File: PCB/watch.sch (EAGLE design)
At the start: 5 parts

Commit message: base layout
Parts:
- removed U$2: 5-WAYSWITCH, 5-wayswitch:5-WAYSWITCH
- added C2: (no value), SparkFun:CAP0603
- added IC1: ISL1209, adafruit:ISL1209
- added Q1: IRFD9210, transistor-fet:IRFD9210
- added SP1: SPEAKER/PS12, adafruit:SPEAKER/PS12
- added U$3: 5-WAYSWITCH, 5-wayswitch:5-WAYSWITCH
- added U1: (no value), adafruit:GPS_FGPMMOPA6H
- added U2: MKL27Z256VLH4, Freescale:MKL27Z256VLH4
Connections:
- new net N$2: Q1.G, U2.PTC1/LLWU_P6/RTC_CLKIN
- new net N$4: U1.TX, U2.PTA19
- new net N$5: SP1.+, U2.PTE30
- new net N$6: Q1.D, U1.VCC
- new net PBT16: U1.3D-FIX
- new net PTB16: U2.PTB16
- net GND: now also C2.2, SP1.-, U$3.GND, U1.GND@1, U1.GND@2, U1.GND@3, U1.GND@4, U2.VSS, U2.VSS_3; no longer U$2.GND
- net V+: now also C2.1, Q1.S, U1.VBACKUP
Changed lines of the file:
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@@
 <layer number="54" name="bGND_GNDA" color="1" fill="9" visible="no" active="no"/>
 <layer number="56" name="wert" color="7" fill="1" visible="no" active="no"/>
+<layer number="57" name="tCAD" color="7" fill="1" visible="no" active="no"/>
 <layer number="90" name="Modules" color="5" fill="1" visible="yes" active="yes"/>
 <layer number="91" name="Nets" color="2" fill="1" visible="yes" active="yes"/>
@@
 <layer number="132" name="bAdjust" color="7" fill="1" visible="yes" active="yes"/>
 <layer number="144" name="Drill_legend" color="7" fill="1" visible="yes" active="yes"/>
+<layer number="150" name="Notes" color="7" fill="1" visible="no" active="yes"/>
 <layer number="151" name="HeatSink" color="7" fill="1" visible="yes" active="yes"/>
 <layer number="152" name="_bDocu" color="7" fill="1" visible="yes" active="yes"/>
+<layer number="153" name="FabDoc1" color="6" fill="1" visible="no" active="no"/>
+<layer number="154" name="FabDoc2" color="2" fill="1" visible="no" active="no"/>
+<layer number="155" name="FabDoc3" color="7" fill="15" visible="no" active="no"/>
 <layer number="199" name="Contour" color="7" fill="1" visible="yes" active="yes"/>
 <layer number="200" name="200bmp" color="1" fill="10" visible="yes" active="yes"/>
@@
 <part name="SUPPLY2" library="supply2" deviceset="GND" device=""/>
 <part name="SUPPLY3" library="supply2" deviceset="V+" device=""/>
-<part name="U$2" library="5-wayswitch" deviceset="5-WAYSWITCH" device=""/>
 <part name="SUPPLY4" library="supply2" deviceset="GND" device=""/>
+<part name="U1" library="adafruit" deviceset="GPS_FGPMMOPA6H" device=""/>
+<part name="SUPPLY5" library="supply2" deviceset="GND" device=""/>
+<part name="U2" library="Freescale" deviceset="MKL27Z256VLH4" device=""/>
+<part name="SUPPLY6" library="supply2" deviceset="GND" device=""/>
+<part name="SUPPLY7" library="supply2" deviceset="GND" device=""/>
+<part name="C2" library="SparkFun" deviceset="CAP" device="0603"/>
+<part name="SUPPLY8" library="supply2" deviceset="V+" device=""/>
+<part name="SUPPLY9" library="supply2" deviceset="GND" device=""/>
+<part name="SUPPLY10" library="supply2" deviceset="V+" device=""/>
+<part name="Q1" library="transistor-fet" deviceset="IRFD9210" device=""/>
+<part name="U$3" library="5-wayswitch" deviceset="5-WAYSWITCH" device=""/>
+<part name="SP1" library="adafruit" deviceset="SPEAKER" device="/PS12"/>
+<part name="IC1" library="adafruit" deviceset="ISL1209" device=""/>
 </parts>
 <sheets>
@@
 </plain>
 <instances>
-<instance part="DISP1" gate="G$1" x="-5.08" y="35.56"/>
-<instance part="DISP2" gate="G$1" x="66.04" y="35.56"/>
+<instance part="DISP1" gate="G$1" x="-10.16" y="195.58"/>
+<instance part="DISP2" gate="G$1" x="60.96" y="195.58"/>
 <instance part="U$1" gate="G$1" x="-88.9" y="83.82"/>
 <instance part="C1" gate="G$1" x="-63.5" y="101.6"/>
@@
 <instance part="SUPPLY2" gate="GND" x="-63.5" y="93.98"/>
 <instance part="SUPPLY3" gate="1" x="-63.5" y="114.3"/>
-<instance part="U$2" gate="G$1" x="25.4" y="-20.32"/>
-<instance part="SUPPLY4" gate="GND" x="55.88" y="-27.94" rot="R90"/>
+<instance part="SUPPLY4" gate="GND" x="58.42" y="55.88" rot="R90"/>
+<instance part="U1" gate="G$1" x="160.02" y="91.44"/>
+<instance part="SUPPLY5" gate="GND" x="119.38" y="96.52" rot="R270"/>
+<instance part="U2" gate="A" x="-25.4" y="162.56"/>
+<instance part="SUPPLY6" gate="GND" x="-53.34" y="86.36" rot="R270"/>
+<instance part="SUPPLY7" gate="GND" x="99.06" y="119.38" rot="R90"/>
+<instance part="C2" gate="G$1" x="111.76" y="104.14" rot="R90"/>
+<instance part="SUPPLY8" gate="1" x="101.6" y="104.14" rot="R90"/>
+<instance part="SUPPLY9" gate="GND" x="119.38" y="104.14" rot="R90"/>
+<instance part="SUPPLY10" gate="1" x="137.16" y="111.76"/>
+<instance part="Q1" gate="G$1" x="124.46" y="114.3"/>
+<instance part="U$3" gate="G$1" x="25.4" y="63.5"/>
+<instance part="SP1" gate="S1" x="-45.72" y="106.68" rot="R270"/>
+<instance part="IC1" gate="G$1" x="-109.22" y="121.92"/>
 </instances>
 <busses>
@@
 </segment>
 <segment>
-<pinref part="U$2" gate="G$1" pin="GND"/>
 <pinref part="SUPPLY4" gate="GND" pin="GND"/>
-<wire x1="38.1" y1="-25.4" x2="53.34" y2="-25.4" width="0.1524" layer="91"/>
-<wire x1="53.34" y1="-25.4" x2="53.34" y2="-27.94" width="0.1524" layer="91"/>
+<wire x1="38.1" y1="58.42" x2="55.88" y2="58.42" width="0.1524" layer="91"/>
+<wire x1="55.88" y1="58.42" x2="55.88" y2="55.88" width="0.1524" layer="91"/>
+<pinref part="U$3" gate="G$1" pin="GND"/>
+</segment>
+<segment>
+<pinref part="U1" gate="G$1" pin="GND@1"/>
+<pinref part="SUPPLY5" gate="GND" pin="GND"/>
+<wire x1="144.78" y1="96.52" x2="132.08" y2="96.52" width="0.1524" layer="91"/>
+<pinref part="U1" gate="G$1" pin="GND@3"/>
+<wire x1="132.08" y1="96.52" x2="124.46" y2="96.52" width="0.1524" layer="91"/>
+<wire x1="124.46" y1="96.52" x2="121.92" y2="96.52" width="0.1524" layer="91"/>
+<wire x1="175.26" y1="81.28" x2="195.58" y2="81.28" width="0.1524" layer="91"/>
+<wire x1="195.58" y1="81.28" x2="195.58" y2="99.06" width="0.1524" layer="91"/>
+<wire x1="195.58" y1="99.06" x2="195.58" y2="119.38" width="0.1524" layer="91"/>
+<wire x1="195.58" y1="119.38" x2="132.08" y2="119.38" width="0.1524" layer="91"/>
+<wire x1="132.08" y1="119.38" x2="132.08" y2="96.52" width="0.1524" layer="91"/>
+<junction x="132.08" y="96.52"/>
+<pinref part="U1" gate="G$1" pin="GND@4"/>
+<wire x1="175.26" y1="99.06" x2="195.58" y2="99.06" width="0.1524" layer="91"/>
+<junction x="195.58" y="99.06"/>
+<pinref part="U1" gate="G$1" pin="GND@2"/>
+<wire x1="144.78" y1="83.82" x2="124.46" y2="83.82" width="0.1524" layer="91"/>
+<wire x1="124.46" y1="83.82" x2="124.46" y2="96.52" width="0.1524" layer="91"/>
+<junction x="124.46" y="96.52"/>
+</segment>
+<segment>
+<pinref part="C2" gate="G$1" pin="2"/>
+<pinref part="SUPPLY9" gate="GND" pin="GND"/>
+<wire x1="114.3" y1="104.14" x2="116.84" y2="104.14" width="0.1524" layer="91"/>
+</segment>
+<segment>
+<pinref part="SUPPLY6" gate="GND" pin="GND"/>
+<pinref part="U2" gate="A" pin="VSS_3"/>
+<wire x1="-50.8" y1="86.36" x2="-45.72" y2="86.36" width="0.1524" layer="91"/>
+<pinref part="SP1" gate="S1" pin="-"/>
+<wire x1="-45.72" y1="86.36" x2="-25.4" y2="86.36" width="0.1524" layer="91"/>
+<wire x1="-45.72" y1="101.6" x2="-45.72" y2="86.36" width="0.1524" layer="91"/>
+<junction x="-45.72" y="86.36"/>
+</segment>
+<segment>
+<pinref part="U2" gate="A" pin="VSS"/>
+<pinref part="SUPPLY7" gate="GND" pin="GND"/>
+<wire x1="81.28" y1="119.38" x2="96.52" y2="119.38" width="0.1524" layer="91"/>
 </segment>
 </net>
@@
 <wire x1="-63.5" y1="106.68" x2="-63.5" y2="111.76" width="0.1524" layer="91"/>
 </segment>
-</net>
+<segment>
+<pinref part="SUPPLY8" gate="1" pin="V+"/>
+<pinref part="C2" gate="G$1" pin="1"/>
+<wire x1="104.14" y1="104.14" x2="106.68" y2="104.14" width="0.1524" layer="91"/>
+</segment>
+<segment>
+<pinref part="SUPPLY10" gate="1" pin="V+"/>
+<pinref part="U1" gate="G$1" pin="VBACKUP"/>
+<wire x1="144.78" y1="93.98" x2="137.16" y2="93.98" width="0.1524" layer="91"/>
+<wire x1="137.16" y1="93.98" x2="137.16" y2="104.14" width="0.1524" layer="91"/>
+<pinref part="Q1" gate="G$1" pin="S"/>
+<wire x1="137.16" y1="104.14" x2="137.16" y2="109.22" width="0.1524" layer="91"/>
+<wire x1="129.54" y1="111.76" x2="129.54" y2="104.14" width="0.1524" layer="91"/>
+<wire x1="129.54" y1="104.14" x2="137.16" y2="104.14" width="0.1524" layer="91"/>
+<junction x="137.16" y="104.14"/>
+</segment>
+</net>
+<net name="N$4" class="0">
+<segment>
+<pinref part="U1" gate="G$1" pin="TX"/>
+<wire x1="144.78" y1="81.28" x2="83.82" y2="81.28" width="0.1524" layer="91"/>
+<wire x1="83.82" y1="81.28" x2="83.82" y2="83.82" width="0.1524" layer="91"/>
+<pinref part="U2" gate="A" pin="PTA19"/>
+<wire x1="83.82" y1="83.82" x2="81.28" y2="83.82" width="0.1524" layer="91"/>
+</segment>
+</net>
+<net name="N$2" class="0">
+<segment>
+<pinref part="Q1" gate="G$1" pin="G"/>
+<pinref part="U2" gate="A" pin="PTC1/LLWU_P6/RTC_CLKIN"/>
+<wire x1="119.38" y1="111.76" x2="81.28" y2="111.76" width="0.1524" layer="91"/>
+</segment>
+</net>
+<net name="N$6" class="0">
+<segment>
+<pinref part="U1" gate="G$1" pin="VCC"/>
+<wire x1="144.78" y1="101.6" x2="144.78" y2="116.84" width="0.1524" layer="91"/>
+<pinref part="Q1" gate="G$1" pin="D"/>
+<wire x1="144.78" y1="116.84" x2="129.54" y2="116.84" width="0.1524" layer="91"/>
+</segment>
+</net>
+<net name="N$5" class="0">
+<segment>
+<pinref part="U2" gate="A" pin="PTE30"/>
+<pinref part="SP1" gate="S1" pin="+"/>
+<wire x1="-45.72" y1="119.38" x2="-45.72" y2="111.76" width="0.1524" layer="91"/>
+<wire x1="-25.4" y1="119.38" x2="-45.72" y2="119.38" width="0.1524" layer="91"/>
+</segment>
+</net>
+<net name="PTB16" class="0">
+<segment>
+<pinref part="U2" gate="A" pin="PTB16"/>
+<wire x1="81.28" y1="99.06" x2="83.82" y2="99.06" width="0.1524" layer="91"/>
+<junction x="83.82" y="99.06"/>
+</segment>
+</net>
+<net name="PBT16" class="0">
+<segment>
+<pinref part="U1" gate="G$1" pin="3D-FIX"/>
+<wire x1="144.78" y1="91.44" x2="137.16" y2="91.44" width="0.1524" layer="91"/>
+<label x="137.16" y="91.44" size="1.778" layer="95" rot="R180"/>
+</segment>
+</net>

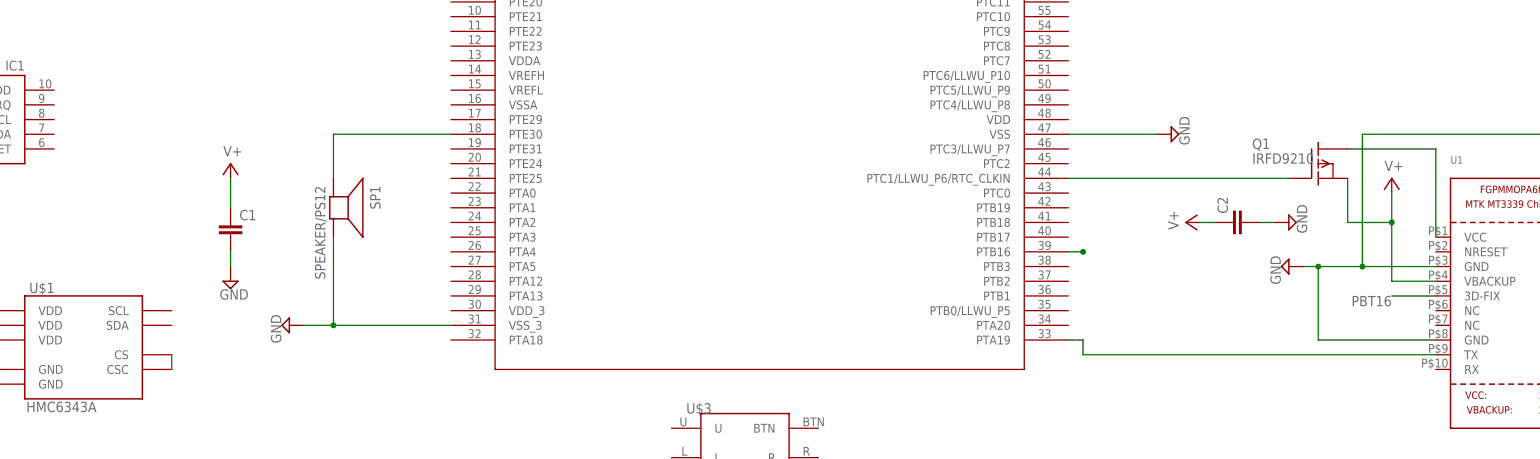
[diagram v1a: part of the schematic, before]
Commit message: made less messy, added libs
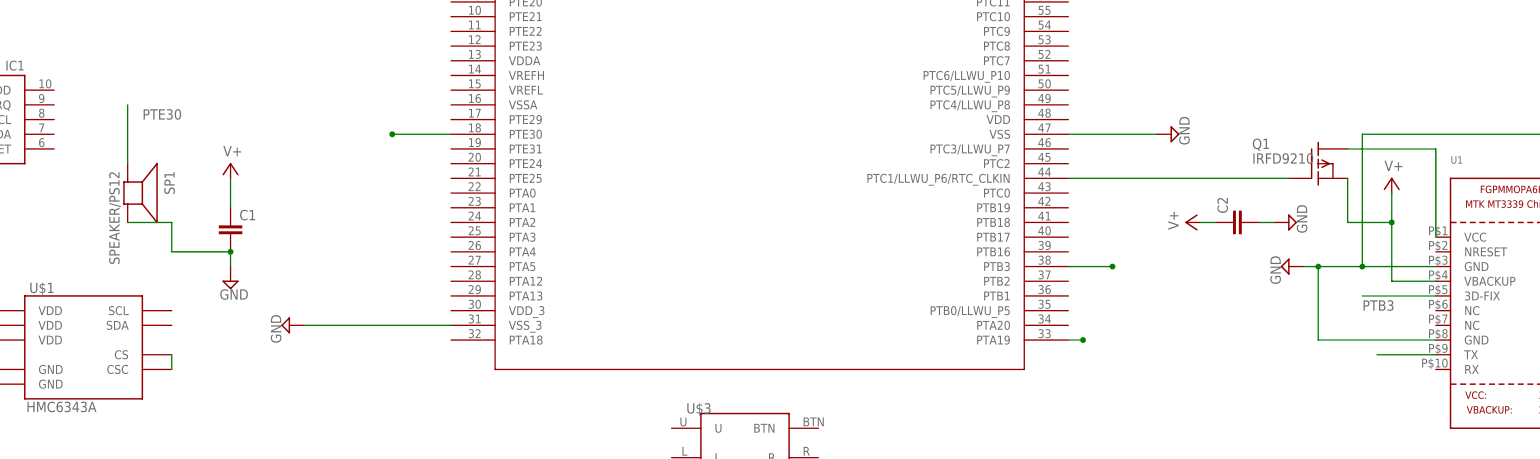
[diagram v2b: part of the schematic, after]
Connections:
- net N$4 renamed PTA19
- net N$5 renamed PTE30
- removed net PBT16: U1.3D-FIX
- removed net PTB16: U2.PTB16
- new net PTB3: U1.3D-FIX, U2.PTB3
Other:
- moved on the sheet: SP1
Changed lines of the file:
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@@
 <instance part="Q1" gate="G$1" x="124.46" y="114.3"/>
 <instance part="U$3" gate="G$1" x="25.4" y="63.5"/>
-<instance part="SP1" gate="S1" x="-45.72" y="106.68" rot="R270"/>
+<instance part="SP1" gate="S1" x="-81.28" y="109.22" rot="R270"/>
 <instance part="IC1" gate="G$1" x="-109.22" y="121.92"/>
 </instances>
@@
 <pinref part="SUPPLY2" gate="GND" pin="GND"/>
 <pinref part="C1" gate="G$1" pin="2"/>
-<wire x1="-63.5" y1="96.52" x2="-63.5" y2="99.06" width="0.1524" layer="91"/>
+<pinref part="SP1" gate="S1" pin="-"/>
+<wire x1="-81.28" y1="104.14" x2="-73.66" y2="104.14" width="0.1524" layer="91"/>
+<wire x1="-73.66" y1="104.14" x2="-73.66" y2="99.06" width="0.1524" layer="91"/>
+<wire x1="-73.66" y1="99.06" x2="-63.5" y2="99.06" width="0.1524" layer="91"/>
+<wire x1="-63.5" y1="99.06" x2="-63.5" y2="96.52" width="0.1524" layer="91"/>
+<junction x="-63.5" y="99.06"/>
 </segment>
 <segment>
@@
 <pinref part="SUPPLY6" gate="GND" pin="GND"/>
 <pinref part="U2" gate="A" pin="VSS_3"/>
-<wire x1="-50.8" y1="86.36" x2="-45.72" y2="86.36" width="0.1524" layer="91"/>
-<pinref part="SP1" gate="S1" pin="-"/>
-<wire x1="-45.72" y1="86.36" x2="-25.4" y2="86.36" width="0.1524" layer="91"/>
-<wire x1="-45.72" y1="101.6" x2="-45.72" y2="86.36" width="0.1524" layer="91"/>
-<junction x="-45.72" y="86.36"/>
+<wire x1="-50.8" y1="86.36" x2="-25.4" y2="86.36" width="0.1524" layer="91"/>
 </segment>
 <segment>
@@
 </segment>
 </net>
-<net name="N$4" class="0">
+<net name="PTA19" class="0">
+<segment>
+<pinref part="U2" gate="A" pin="PTA19"/>
+<wire x1="83.82" y1="83.82" x2="81.28" y2="83.82" width="0.1524" layer="91"/>
+<junction x="83.82" y="83.82"/>
+</segment>
 <segment>
 <pinref part="U1" gate="G$1" pin="TX"/>
-<wire x1="144.78" y1="81.28" x2="83.82" y2="81.28" width="0.1524" layer="91"/>
-<wire x1="83.82" y1="81.28" x2="83.82" y2="83.82" width="0.1524" layer="91"/>
-<pinref part="U2" gate="A" pin="PTA19"/>
-<wire x1="83.82" y1="83.82" x2="81.28" y2="83.82" width="0.1524" layer="91"/>
+<wire x1="144.78" y1="81.28" x2="134.62" y2="81.28" width="0.1524" layer="91"/>
 </segment>
 </net>
@@
 </segment>
 </net>
-<net name="N$5" class="0">
+<net name="PTB3" class="0">
+<segment>
+<pinref part="U2" gate="A" pin="PTB3"/>
+<wire x1="88.9" y1="96.52" x2="81.28" y2="96.52" width="0.1524" layer="91"/>
+<junction x="88.9" y="96.52"/>
+</segment>
+<segment>
+<pinref part="U1" gate="G$1" pin="3D-FIX"/>
+<wire x1="144.78" y1="91.44" x2="132.08" y2="91.44" width="0.1524" layer="91"/>
+<label x="132.08" y="88.9" size="1.778" layer="95"/>
+</segment>
+</net>
+<net name="PTE30" class="0">
+<segment>
+<pinref part="SP1" gate="S1" pin="+"/>
+<wire x1="-81.28" y1="114.3" x2="-81.28" y2="124.46" width="0.1524" layer="91"/>
+<label x="-78.74" y="121.92" size="1.778" layer="95"/>
+</segment>
 <segment>
 <pinref part="U2" gate="A" pin="PTE30"/>
-<pinref part="SP1" gate="S1" pin="+"/>
-<wire x1="-45.72" y1="119.38" x2="-45.72" y2="111.76" width="0.1524" layer="91"/>
-<wire x1="-25.4" y1="119.38" x2="-45.72" y2="119.38" width="0.1524" layer="91"/>
+<wire x1="-25.4" y1="119.38" x2="-35.56" y2="119.38" width="0.1524" layer="91"/>
+<junction x="-35.56" y="119.38"/>
 </segment>
 </net>
-<net name="PTB16" class="0">
-<segment>
-<pinref part="U2" gate="A" pin="PTB16"/>
-<wire x1="81.28" y1="99.06" x2="83.82" y2="99.06" width="0.1524" layer="91"/>
-<junction x="83.82" y="99.06"/>
-</segment>
-</net>
-<net name="PBT16" class="0">
-<segment>
-<pinref part="U1" gate="G$1" pin="3D-FIX"/>
-<wire x1="144.78" y1="91.44" x2="137.16" y2="91.44" width="0.1524" layer="91"/>
-<label x="137.16" y="91.44" size="1.778" layer="95" rot="R180"/>
-</segment>
-</net>
